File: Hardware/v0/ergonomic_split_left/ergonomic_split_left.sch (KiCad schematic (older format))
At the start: 0 parts

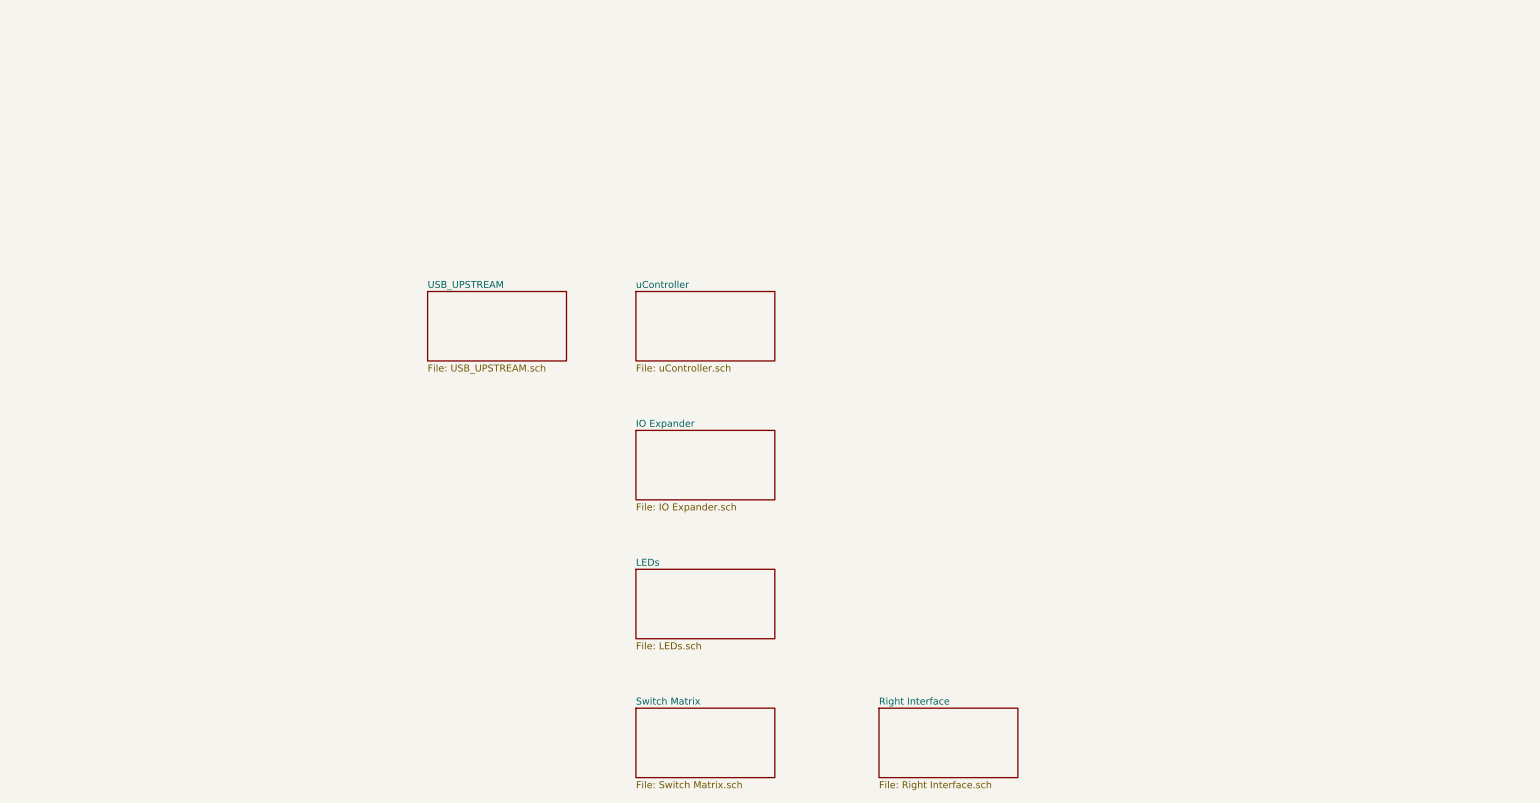
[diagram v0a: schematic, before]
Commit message: Connecting schematic blocks, most sub-blocks done
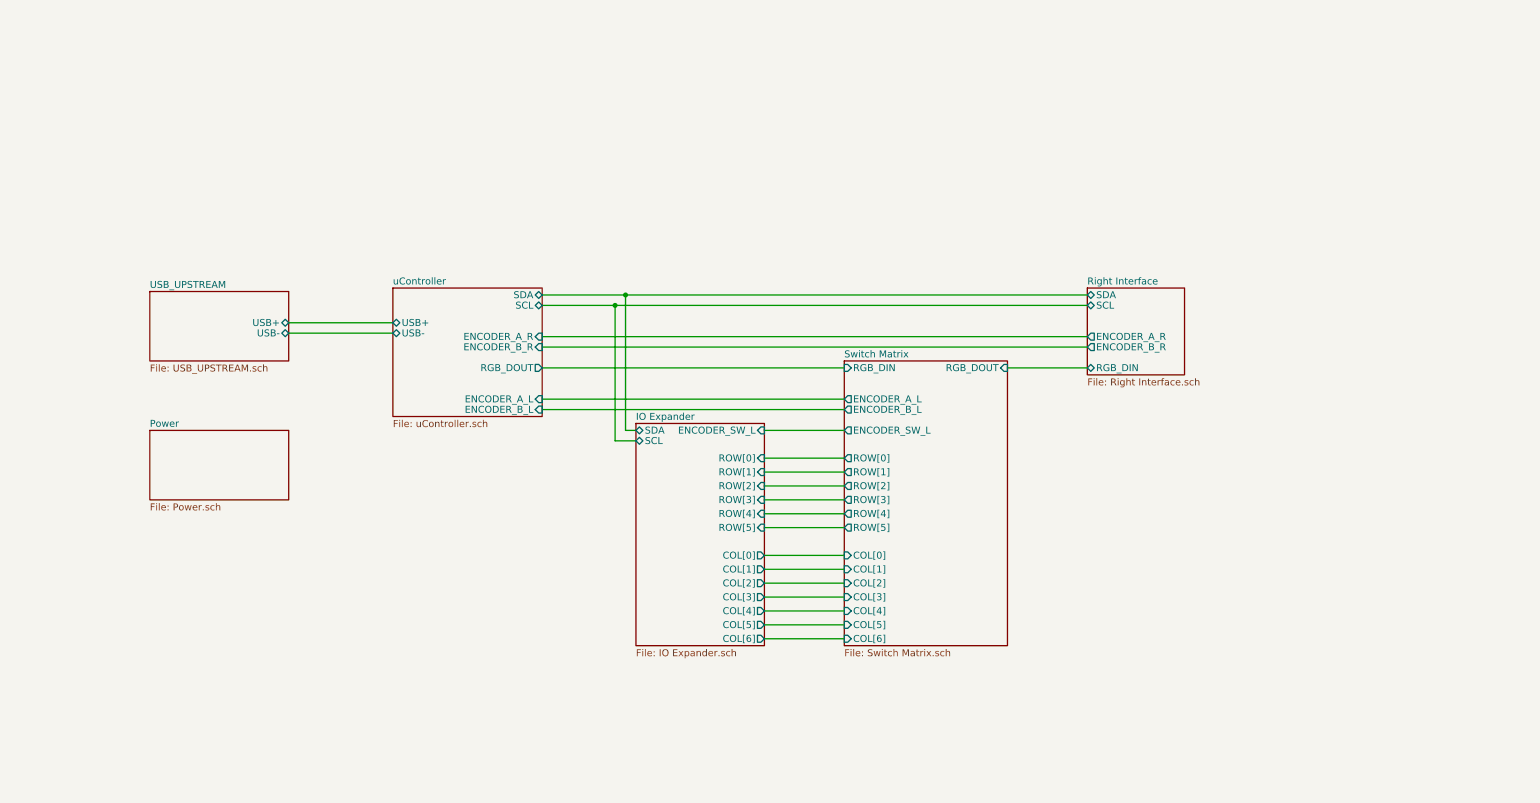
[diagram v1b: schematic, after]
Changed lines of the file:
@@
 $EndDescr
 $Sheet
-S 3750 2500 1000 500
+S 5250 3450 925  1600
+U 629997F8
+F0 "IO Expander" 50
+F1 "IO Expander.sch" 50
+F2 "SDA" B L 5250 3500 50
+F3 "SCL" B L 5250 3575 50
+F4 "ROW[0]" I R 6175 3700 50
+F5 "ROW[1]" I R 6175 3800 50
+F6 "ROW[2]" I R 6175 3900 50
+F7 "ROW[3]" I R 6175 4000 50
+F8 "ROW[4]" I R 6175 4100 50
+F9 "ROW[5]" I R 6175 4200 50
+F10 "COL[0]" O R 6175 4400 50
+F11 "COL[1]" O R 6175 4500 50
+F12 "COL[2]" O R 6175 4600 50
+F13 "COL[3]" O R 6175 4700 50
+F14 "COL[4]" O R 6175 4800 50
+F15 "COL[5]" O R 6175 4900 50
+F16 "COL[6]" O R 6175 5000 50
+F17 "ENCODER_SW_L" I R 6175 3500 50
+$EndSheet
+$Sheet
+S 8500 2475 700  625
+U 62999A71
+F0 "Right Interface" 50
+F1 "Right Interface.sch" 50
+F2 "ENCODER_A_R" O L 8500 2825 50
+F3 "ENCODER_B_R" O L 8500 2900 50
+F4 "SDA" B L 8500 2525 50
+F5 "SCL" B L 8500 2600 50
+F6 "RGB_DIN" B L 8500 3050 50
+$EndSheet
+Wire Wire Line
+	7925 3050 8500 3050
+$Sheet
+S 6750 3000 1175 2050
+U 62999965
+F0 "Switch Matrix" 50
+F1 "Switch Matrix.sch" 50
+F2 "RGB_DIN" I L 6750 3050 50
+F3 "ENCODER_SW_L" O L 6750 3500 50
+F4 "ENCODER_A_L" O L 6750 3275 50
+F5 "ENCODER_B_L" O L 6750 3350 50
+F6 "ROW[0]" O L 6750 3700 50
+F7 "ROW[1]" O L 6750 3800 50
+F8 "ROW[2]" O L 6750 3900 50
+F9 "ROW[3]" O L 6750 4000 50
+F10 "ROW[4]" O L 6750 4100 50
+F11 "ROW[5]" O L 6750 4200 50
+F12 "COL[0]" I L 6750 4400 50
+F13 "COL[1]" I L 6750 4500 50
+F14 "COL[2]" I L 6750 4600 50
+F15 "COL[3]" I L 6750 4700 50
+F16 "COL[4]" I L 6750 4800 50
+F17 "COL[5]" I L 6750 4900 50
+F18 "COL[6]" I L 6750 5000 50
+F19 "RGB_DOUT" I R 7925 3050 50
+$EndSheet
+Wire Wire Line
+	6175 3500 6750 3500
+Wire Wire Line
+	6175 3700 6750 3700
+Wire Wire Line
+	6175 3800 6750 3800
+Wire Wire Line
+	6175 3900 6750 3900
+Wire Wire Line
+	6175 4000 6750 4000
+Wire Wire Line
+	6175 4100 6750 4100
+Wire Wire Line
+	6175 4200 6750 4200
+Wire Wire Line
+	6175 4400 6750 4400
+Wire Wire Line
+	6175 4500 6750 4500
+Wire Wire Line
+	6175 4600 6750 4600
+Wire Wire Line
+	6175 4700 6750 4700
+Wire Wire Line
+	6175 4800 6750 4800
+Wire Wire Line
+	6175 4900 6750 4900
+Wire Wire Line
+	6175 5000 6750 5000
+Wire Wire Line
+	2750 2800 3500 2800
+Wire Wire Line
+	3500 2725 2750 2725
+$Sheet
+S 3500 2475 1075 925
+U 62999575
+F0 "uController" 50
+F1 "uController.sch" 50
+F2 "RGB_DOUT" O R 4575 3050 50
+F3 "SDA" B R 4575 2525 50
+F4 "SCL" B R 4575 2600 50
+F5 "USB+" B L 3500 2725 50
+F6 "USB-" B L 3500 2800 50
+F7 "ENCODER_A_R" I R 4575 2825 50
+F8 "ENCODER_B_R" I R 4575 2900 50
+F9 "ENCODER_A_L" I R 4575 3275 50
+F10 "ENCODER_B_L" I R 4575 3350 50
+$EndSheet
+$Sheet
+S 1750 3500 1000 500
+U 6D0600A2
+F0 "Power" 50
+F1 "Power.sch" 50
+$EndSheet
+$Sheet
+S 1750 2500 1000 500
 U 629982B4
 F0 "USB_UPSTREAM" 50
 F1 "USB_UPSTREAM.sch" 50
+F2 "USB+" B R 2750 2725 50
+F3 "USB-" B R 2750 2800 50
 $EndSheet
-$Sheet
-S 5250 2500 1000 500
-U 62999575
-F0 "uController" 50
-F1 "uController.sch" 50
-$EndSheet
-$Sheet
-S 5250 3500 1000 500
-U 629997F8
-F0 "IO Expander" 50
-F1 "IO Expander.sch" 50
-$EndSheet
-$Sheet
-S 5250 4500 1000 500
-U 629998EF
-F0 "LEDs" 50
-F1 "LEDs.sch" 50
-$EndSheet
-$Sheet
-S 5250 5500 1000 500
-U 62999965
-F0 "Switch Matrix" 50
-F1 "Switch Matrix.sch" 50
-$EndSheet
-$Sheet
-S 7000 5500 1000 500
-U 62999A71
-F0 "Right Interface" 50
-F1 "Right Interface.sch" 50
-$EndSheet
+Wire Wire Line
+	4575 3275 6750 3275
+Wire Wire Line
+	4575 3350 6750 3350
+Wire Wire Line
+	4575 3050 6750 3050
+Wire Wire Line
+	4575 2825 8500 2825
+Wire Wire Line
+	4575 2900 8500 2900
+Wire Wire Line
+	4575 2525 5175 2525
+Wire Wire Line
+	4575 2600 5100 2600
+Wire Wire Line
+	5250 3500 5175 3500
+Wire Wire Line
+	5175 3500 5175 2525
+Wire Wire Line
+	5250 3575 5100 3575
+Wire Wire Line
+	5100 3575 5100 2600
+Connection ~ 5100 2600
+Wire Wire Line
+	5100 2600 8500 2600
+Connection ~ 5175 2525
+Wire Wire Line
+	5175 2525 8500 2525
 $EndSCHEMATC

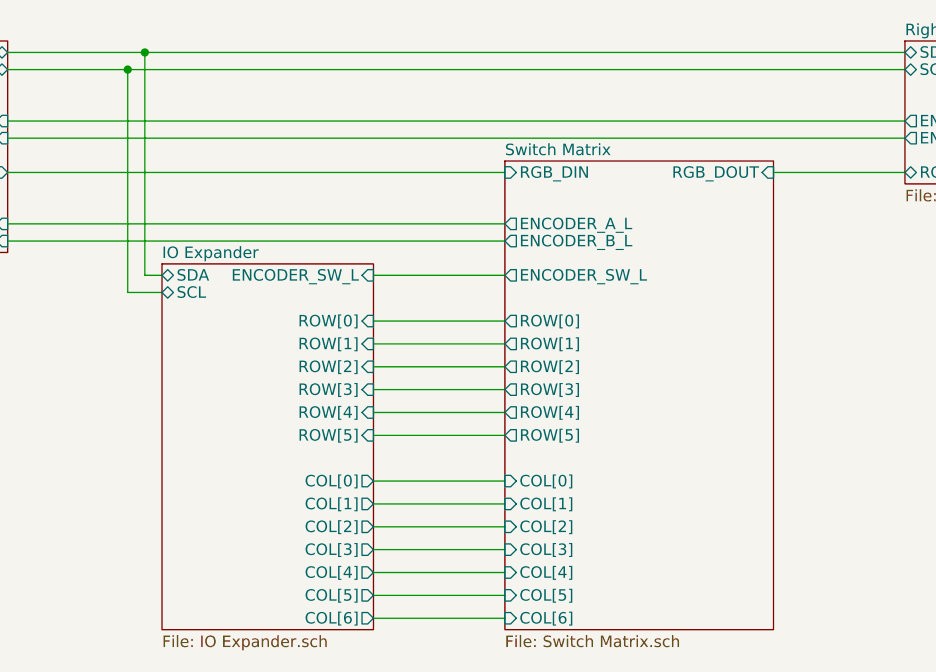
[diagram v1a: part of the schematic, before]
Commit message: Drawing board outline Basic placement done Adding rotary encoder to the switch matrix Adding mounting holes
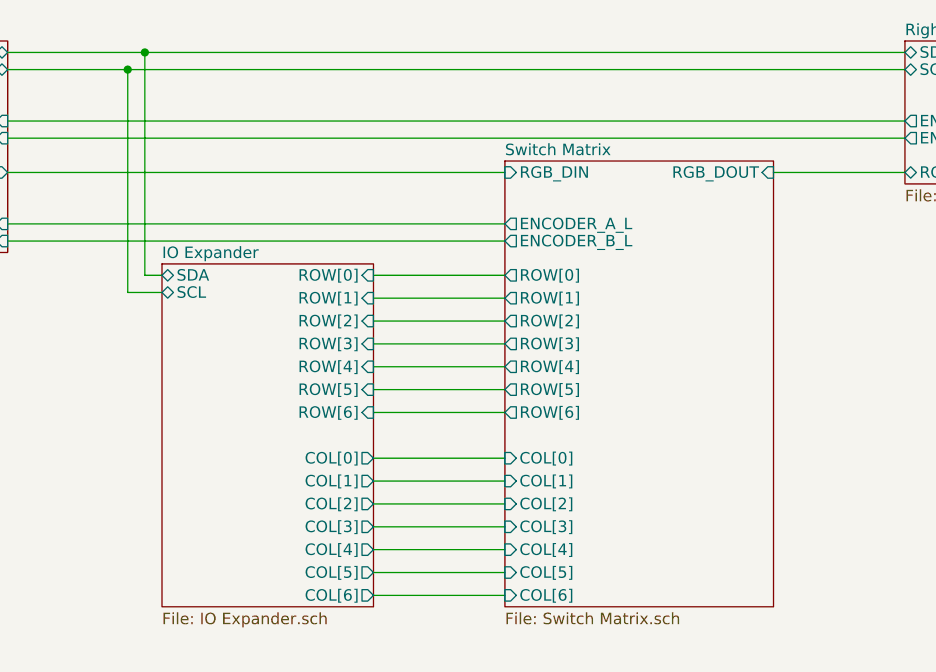
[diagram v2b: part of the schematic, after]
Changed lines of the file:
@@
 $EndDescr
 $Sheet
-S 5250 3450 925  1600
+S 5250 3450 925  1500
 U 629997F8
 F0 "IO Expander" 50
@@
 F2 "SDA" B L 5250 3500 50
 F3 "SCL" B L 5250 3575 50
-F4 "ROW[0]" I R 6175 3700 50
-F5 "ROW[1]" I R 6175 3800 50
-F6 "ROW[2]" I R 6175 3900 50
-F7 "ROW[3]" I R 6175 4000 50
-F8 "ROW[4]" I R 6175 4100 50
-F9 "ROW[5]" I R 6175 4200 50
-F10 "COL[0]" O R 6175 4400 50
-F11 "COL[1]" O R 6175 4500 50
-F12 "COL[2]" O R 6175 4600 50
-F13 "COL[3]" O R 6175 4700 50
-F14 "COL[4]" O R 6175 4800 50
-F15 "COL[5]" O R 6175 4900 50
-F16 "COL[6]" O R 6175 5000 50
-F17 "ENCODER_SW_L" I R 6175 3500 50
+F4 "ROW[0]" I R 6175 3500 50
+F5 "ROW[1]" I R 6175 3600 50
+F6 "ROW[2]" I R 6175 3700 50
+F7 "ROW[3]" I R 6175 3800 50
+F8 "ROW[4]" I R 6175 3900 50
+F9 "ROW[5]" I R 6175 4000 50
+F10 "COL[0]" O R 6175 4300 50
+F11 "COL[1]" O R 6175 4400 50
+F12 "COL[2]" O R 6175 4500 50
+F13 "COL[3]" O R 6175 4600 50
+F14 "COL[4]" O R 6175 4700 50
+F15 "COL[5]" O R 6175 4800 50
+F16 "COL[6]" O R 6175 4900 50
+F17 "ROW[6]" I R 6175 4100 50
 $EndSheet
 $Sheet
@@
 	7925 3050 8500 3050
 $Sheet
-S 6750 3000 1175 2050
+S 6750 3000 1175 1950
 U 62999965
 F0 "Switch Matrix" 50
 F1 "Switch Matrix.sch" 50
 F2 "RGB_DIN" I L 6750 3050 50
-F3 "ENCODER_SW_L" O L 6750 3500 50
+F3 "ROW[6]" O L 6750 4100 50
 F4 "ENCODER_A_L" O L 6750 3275 50
 F5 "ENCODER_B_L" O L 6750 3350 50
-F6 "ROW[0]" O L 6750 3700 50
-F7 "ROW[1]" O L 6750 3800 50
-F8 "ROW[2]" O L 6750 3900 50
-F9 "ROW[3]" O L 6750 4000 50
-F10 "ROW[4]" O L 6750 4100 50
-F11 "ROW[5]" O L 6750 4200 50
-F12 "COL[0]" I L 6750 4400 50
-F13 "COL[1]" I L 6750 4500 50
-F14 "COL[2]" I L 6750 4600 50
-F15 "COL[3]" I L 6750 4700 50
-F16 "COL[4]" I L 6750 4800 50
-F17 "COL[5]" I L 6750 4900 50
-F18 "COL[6]" I L 6750 5000 50
+F6 "ROW[0]" O L 6750 3500 50
+F7 "ROW[1]" O L 6750 3600 50
+F8 "ROW[2]" O L 6750 3700 50
+F9 "ROW[3]" O L 6750 3800 50
+F10 "ROW[4]" O L 6750 3900 50
+F11 "ROW[5]" O L 6750 4000 50
+F12 "COL[0]" I L 6750 4300 50
+F13 "COL[1]" I L 6750 4400 50
+F14 "COL[2]" I L 6750 4500 50
+F15 "COL[3]" I L 6750 4600 50
+F16 "COL[4]" I L 6750 4700 50
+F17 "COL[5]" I L 6750 4800 50
+F18 "COL[6]" I L 6750 4900 50
 F19 "RGB_DOUT" I R 7925 3050 50
 $EndSheet
 Wire Wire Line
 	6175 3500 6750 3500
+Wire Wire Line
+	6175 3600 6750 3600
 Wire Wire Line
 	6175 3700 6750 3700
@@
 	6175 4100 6750 4100
 Wire Wire Line
-	6175 4200 6750 4200
+	6175 4300 6750 4300
 Wire Wire Line
 	6175 4400 6750 4400
@@
 	6175 4900 6750 4900
 Wire Wire Line
-	6175 5000 6750 5000
-Wire Wire Line
 	2750 2800 3500 2800

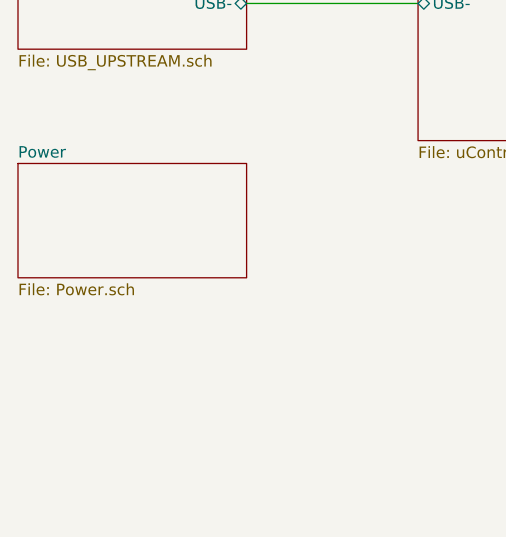
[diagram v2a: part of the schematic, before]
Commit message: Debug connectors Adding I2C debug header Changed SPI programming header to edge mount Changed right interface connector to IDC Cleaning up schematic
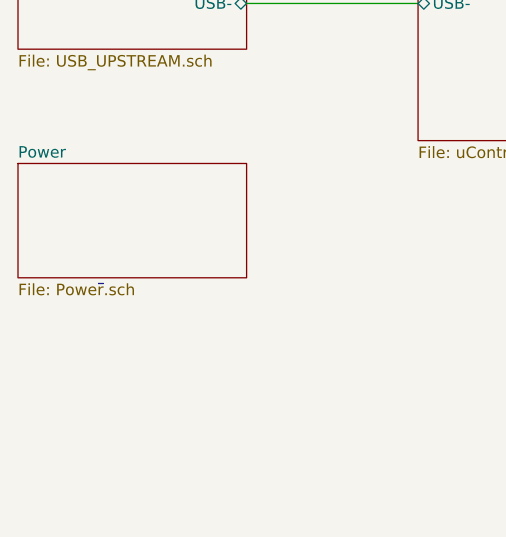
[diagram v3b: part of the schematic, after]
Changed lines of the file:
@@
 Wire Wire Line
 	5175 2525 8500 2525
+Wire Notes Line
+	2100 4025 2125 4025
 $EndSCHEMATC

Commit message: Schematic title page
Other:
- note added: "ergonomic split keyboard - left side"
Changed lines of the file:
@@
 Wire Notes Line
 	2100 4025 2125 4025
+Text Notes 750  1000 0    315  ~ 0
+ergonomic split keyboard - left side
 $EndSCHEMATC
